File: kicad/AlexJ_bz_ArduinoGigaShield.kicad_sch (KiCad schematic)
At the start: 59 parts, among them J1 Conn_01x08, J10 JSIDE_5V, J2 Conn_01x10, J3 Conn_01x08, J4 Conn_01x08, J5 Conn_01x26, J6 Conn_01x08, J7 Conn_01x08, J8 Conn_01x26, J9 JSIDE, U1 TXB0108PW, U2 TXB0108PW, U3 TXB0108PW, U4 TXB0108PW, U5 TXB0108PW, U6 TXB0108PW, U7 TXB0108PW, U8 TXB0108PW, U9 TXB0108PW

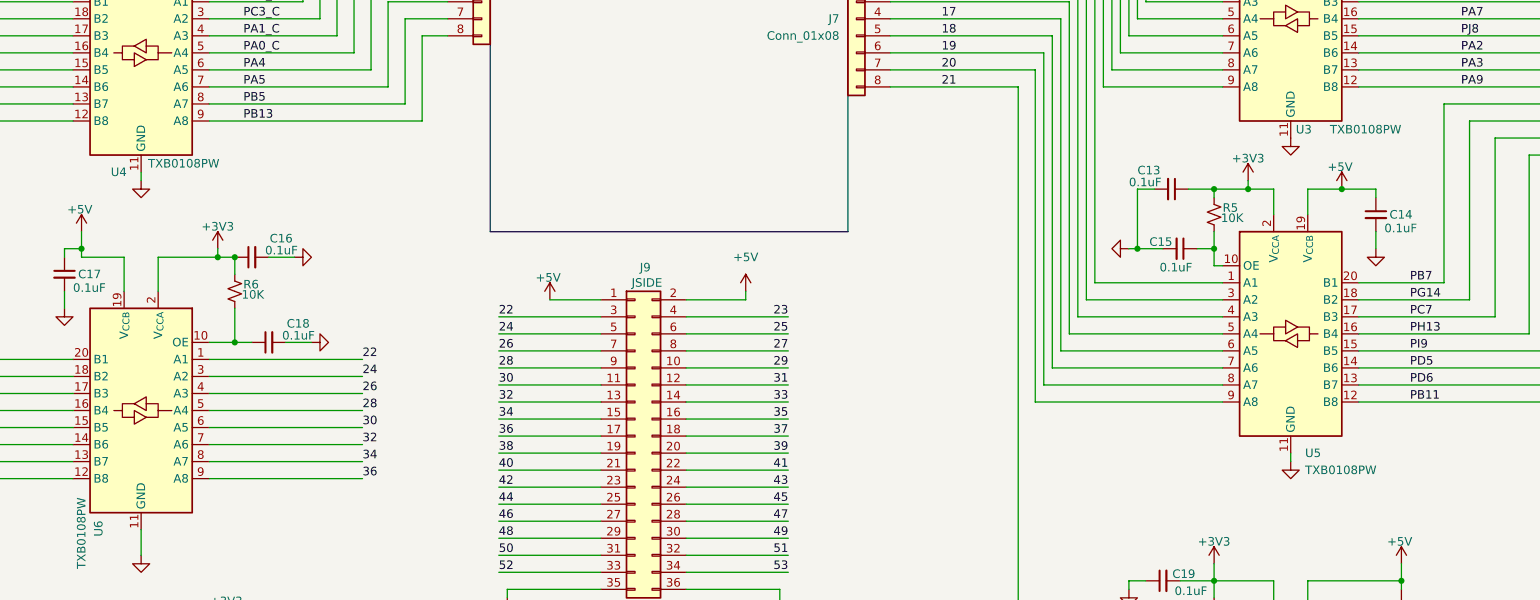
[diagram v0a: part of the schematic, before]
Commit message: Update KiCad schematic and PCB annotations for v0.2 IC replacements
Schematic: Update Value, Datasheet, and Description properties on U1-U5
to reflect new IC types (SN74LVC541, SN74AHCT541, SN74LVC4245A).
Update U5 Footprint property to TSSOP-24.

PCB: Update Value, Datasheet, and Description on U1-U5 footprints.
Update U5 footprint reference to TSSOP-24. Change silkscreen from
V0.1 to V0.2.

Note: lib_symbol definitions, pin mappings, footprint geometry, and
trace routing still reference TXB0108PW and must be updated in
KiCad GUI. See CHANGES-V0.2.md for full implementation guide.
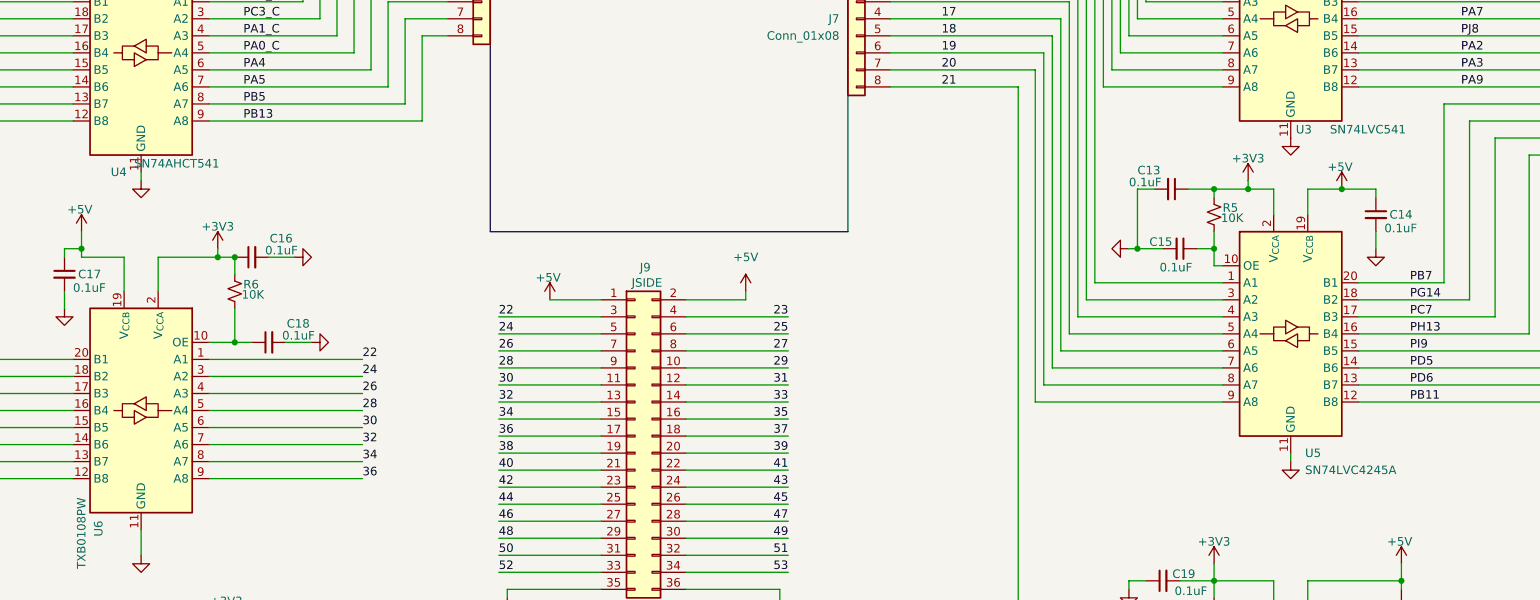
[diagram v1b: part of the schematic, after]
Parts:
- U1, U2, U3: value TXB0108PW -> SN74LVC541
- U4: value TXB0108PW -> SN74AHCT541
- U5: value TXB0108PW -> SN74LVC4245A; footprint Package_SO:TSSOP-20_4.4x6.5mm_P0.65mm -> Package_SO:TSSOP-24_4.4x7.8mm_P0.65mm
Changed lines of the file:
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@@
 			)
 		)
-		(property "Value" "TXB0108PW"
+		(property "Value" "SN74LVC541"
 			(at 100.7267 88.9 0)
 			(effects
@@
 			)
 		)
-		(property "Datasheet" "http://www.ti.com/lit/ds/symlink/txb0108.pdf"
+		(property "Datasheet" "https://www.ti.com/lit/ds/symlink/sn74lvc541a.pdf"
 			(at 102.87 71.12 0)
 			(effects
@@
 			)
 		)
-		(property "Description" "8-Bit Bidirectional Voltage-Level Translator, Auto Direction Sensing and ±15-kV ESD Protection, 1.2 - 3.6V APort, 1.65 - 5.5V BPort, TSSOP-20"
+		(property "Description" "Octal Buffer/Driver With 3-State Outputs, 5V-Tolerant Inputs, TSSOP-20 (v0.2: replaces TXB0108PW for address bus A8-A15)"
 			(at 102.87 68.58 0)
 			(effects
@@
 			)
 		)
-		(property "Value" "TXB0108PW"
+		(property "Value" "SN74LVC541"
 			(at 275.1933 86.36 0)
 			(effects
@@
 			)
 		)
-		(property "Datasheet" "http://www.ti.com/lit/ds/symlink/txb0108.pdf"
+		(property "Datasheet" "https://www.ti.com/lit/ds/symlink/sn74lvc541a.pdf"
 			(at 273.05 68.58 0)
 			(effects
@@
 			)
 		)
-		(property "Description" "8-Bit Bidirectional Voltage-Level Translator, Auto Direction Sensing and ±15-kV ESD Protection, 1.2 - 3.6V APort, 1.65 - 5.5V BPort, TSSOP-20"
+		(property "Description" "Octal Buffer/Driver With 3-State Outputs, 5V-Tolerant Inputs, TSSOP-20 (v0.2: replaces TXB0108PW for address bus A0-A7)"
 			(at 273.05 66.04 0)
 			(effects
@@
 			)
 		)
-		(property "Value" "TXB0108PW"
+		(property "Value" "SN74LVC541"
 			(at 278.892 128.27 0)
 			(effects
@@
 			)
 		)
-		(property "Datasheet" "http://www.ti.com/lit/ds/symlink/txb0108.pdf"
+		(property "Datasheet" "https://www.ti.com/lit/ds/symlink/sn74lvc541a.pdf"
 			(at 273.05 114.3 0)
 			(effects
@@
 			)
 		)
-		(property "Description" "8-Bit Bidirectional Voltage-Level Translator, Auto Direction Sensing and ±15-kV ESD Protection, 1.2 - 3.6V APort, 1.65 - 5.5V BPort, TSSOP-20"
+		(property "Description" "Octal Buffer/Driver With 3-State Outputs, 5V-Tolerant Inputs, TSSOP-20 (v0.2: replaces TXB0108PW for control inputs MREQ/IORQ/RD/WR)"
 			(at 273.05 111.76 0)
 			(effects
@@
 			)
 		)
-		(property "Value" "TXB0108PW"
+		(property "Value" "SN74LVC4245A"
 			(at 275.1933 179.07 0)
 			(effects
@@
 			)
 		)
-		(property "Footprint" "Package_SO:TSSOP-20_4.4x6.5mm_P0.65mm"
+		(property "Footprint" "Package_SO:TSSOP-24_4.4x7.8mm_P0.65mm"
 			(at 273.05 177.8 0)
 			(effects
@@
 			)
 		)
-		(property "Datasheet" "http://www.ti.com/lit/ds/symlink/txb0108.pdf"
+		(property "Datasheet" "https://www.ti.com/lit/ds/symlink/sn74lvc4245a.pdf"
 			(at 273.05 161.29 0)
 			(effects
@@
 			)
 		)
-		(property "Description" "8-Bit Bidirectional Voltage-Level Translator, Auto Direction Sensing and ±15-kV ESD Protection, 1.2 - 3.6V APort, 1.65 - 5.5V BPort, TSSOP-20"
+		(property "Description" "8-Bit Dual-Supply Bus Transceiver With Configurable Voltage Translation and 3-State Outputs, TSSOP-24 (v0.2: replaces TXB0108PW for data bus D0-D7, DIR pin on Arduino D2)"
 			(at 273.05 158.75 0)
 			(effects
@@
 			)
 		)
-		(property "Value" "TXB0108PW"
+		(property "Value" "SN74AHCT541"
 			(at 113.284 133.35 0)
 			(effects
@@
 			)
 		)
-		(property "Datasheet" "http://www.ti.com/lit/ds/symlink/txb0108.pdf"
+		(property "Datasheet" "https://www.ti.com/lit/ds/symlink/sn74ahct541.pdf"
 			(at 101.6 119.38 0)
 			(effects
@@
 			)
 		)
-		(property "Description" "8-Bit Bidirectional Voltage-Level Translator, Auto Direction Sensing and ±15-kV ESD Protection, 1.2 - 3.6V APort, 1.65 - 5.5V BPort, TSSOP-20"
+		(property "Description" "Octal Buffer/Driver With 3-State Outputs, TTL-Compatible Inputs, TSSOP-20 (v0.2: replaces TXB0108PW for control outputs CLK/RESET/INT/NMI)"
 			(at 101.6 116.84 0)
 			(effects

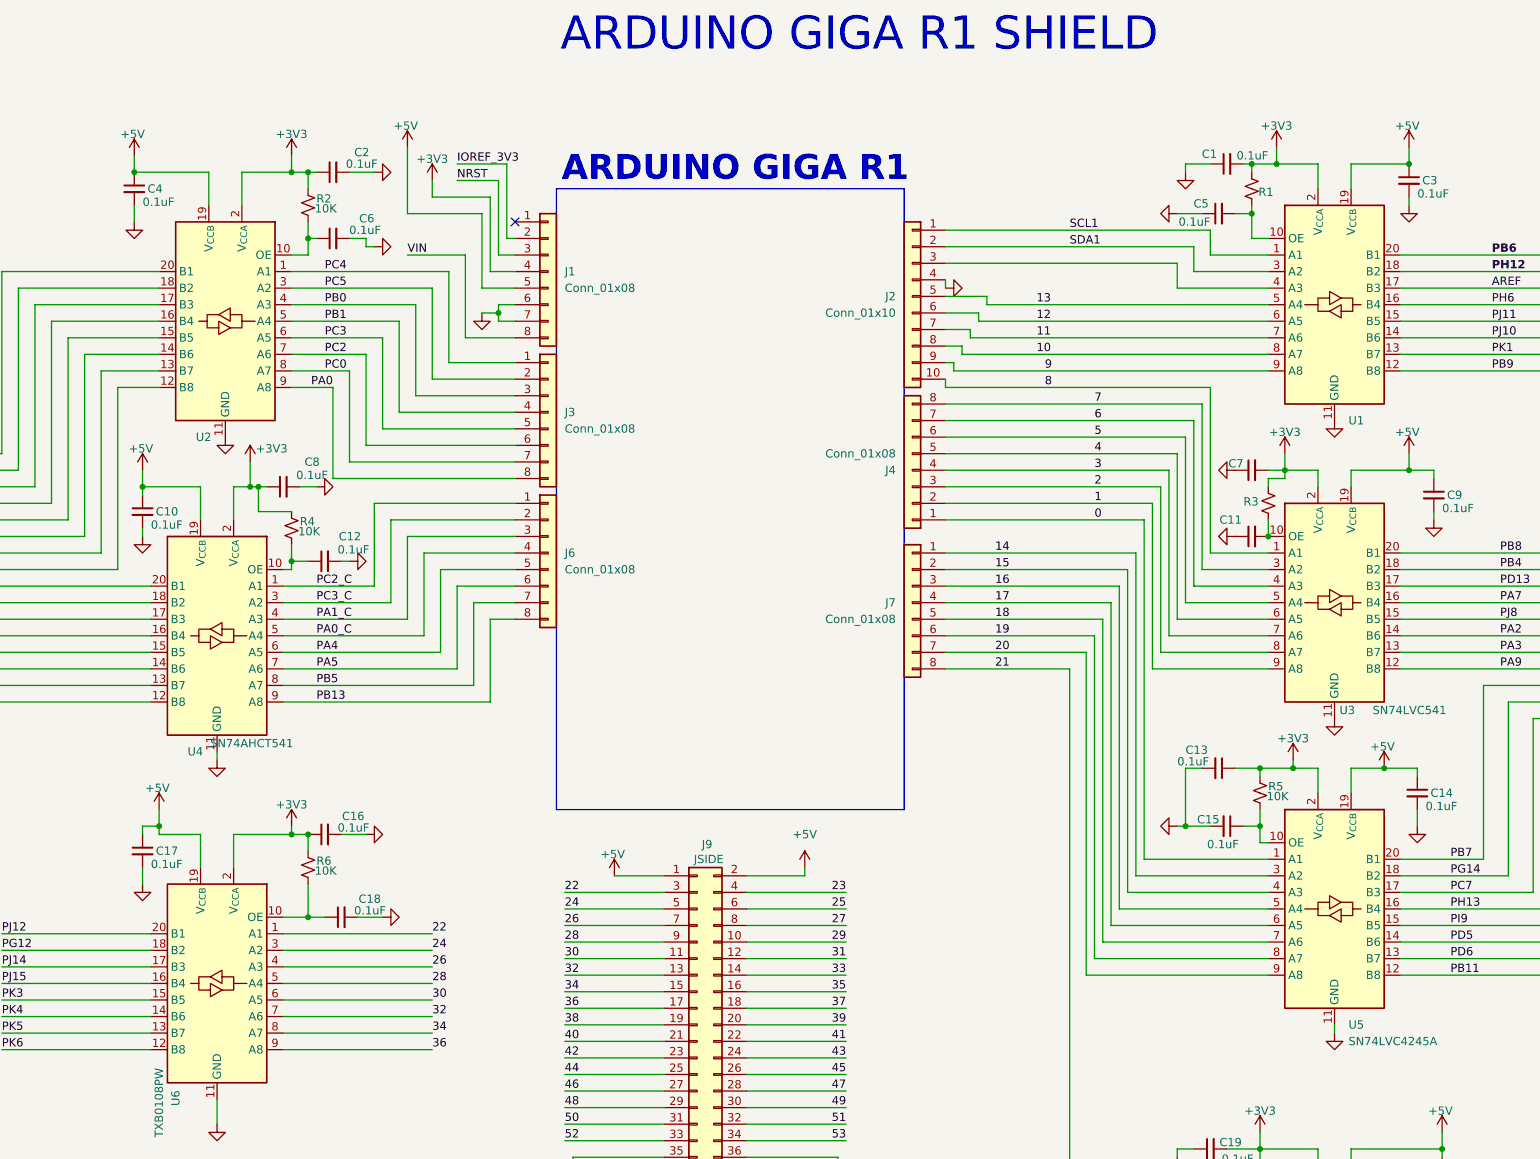
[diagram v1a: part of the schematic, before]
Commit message: v0.2 schematic: replace U1-U5 with purpose-matched level translators
- Replace U1-U3 lib_symbols from TXB0108PW to SN74LVC541 (address bus + control inputs)
- Replace U4 lib_symbol to SN74AHCT541 (control outputs)
- Replace U5 lib_symbol to SN74LVC4245A (bidirectional data bus with DIR)
- Add lib_symbol definitions for SN74LVC541, SN74AHCT541, SN74LVC4245A
- Remove R1-R5 pull-up resistors (OE pins now tied to GND)
- Add GND symbols at 1OE and 2OE pins for U1-U4
- Add GND at U5 OE_N pin (new bottom pin on TSSOP-24)
- Add DATA_DIR net label at U5 DIR pin for Arduino D2 connection
- Change U4 VCC from +3V3 to +5V (AHCT541 runs on 5V rail)
- Replace +5V with GND at VCCB/2OE positions for U1-U3
- Update silkscreen from V0.1 to V0.2
- Update Value/Description/Datasheet properties on U1-U5

Note: C19-C27 (extra decoupling caps) remain in schematic but are
excluded from BOM/CPL. Final cleanup requires KiCad GUI for trace
rerouting, footprint updates, and cap removal.
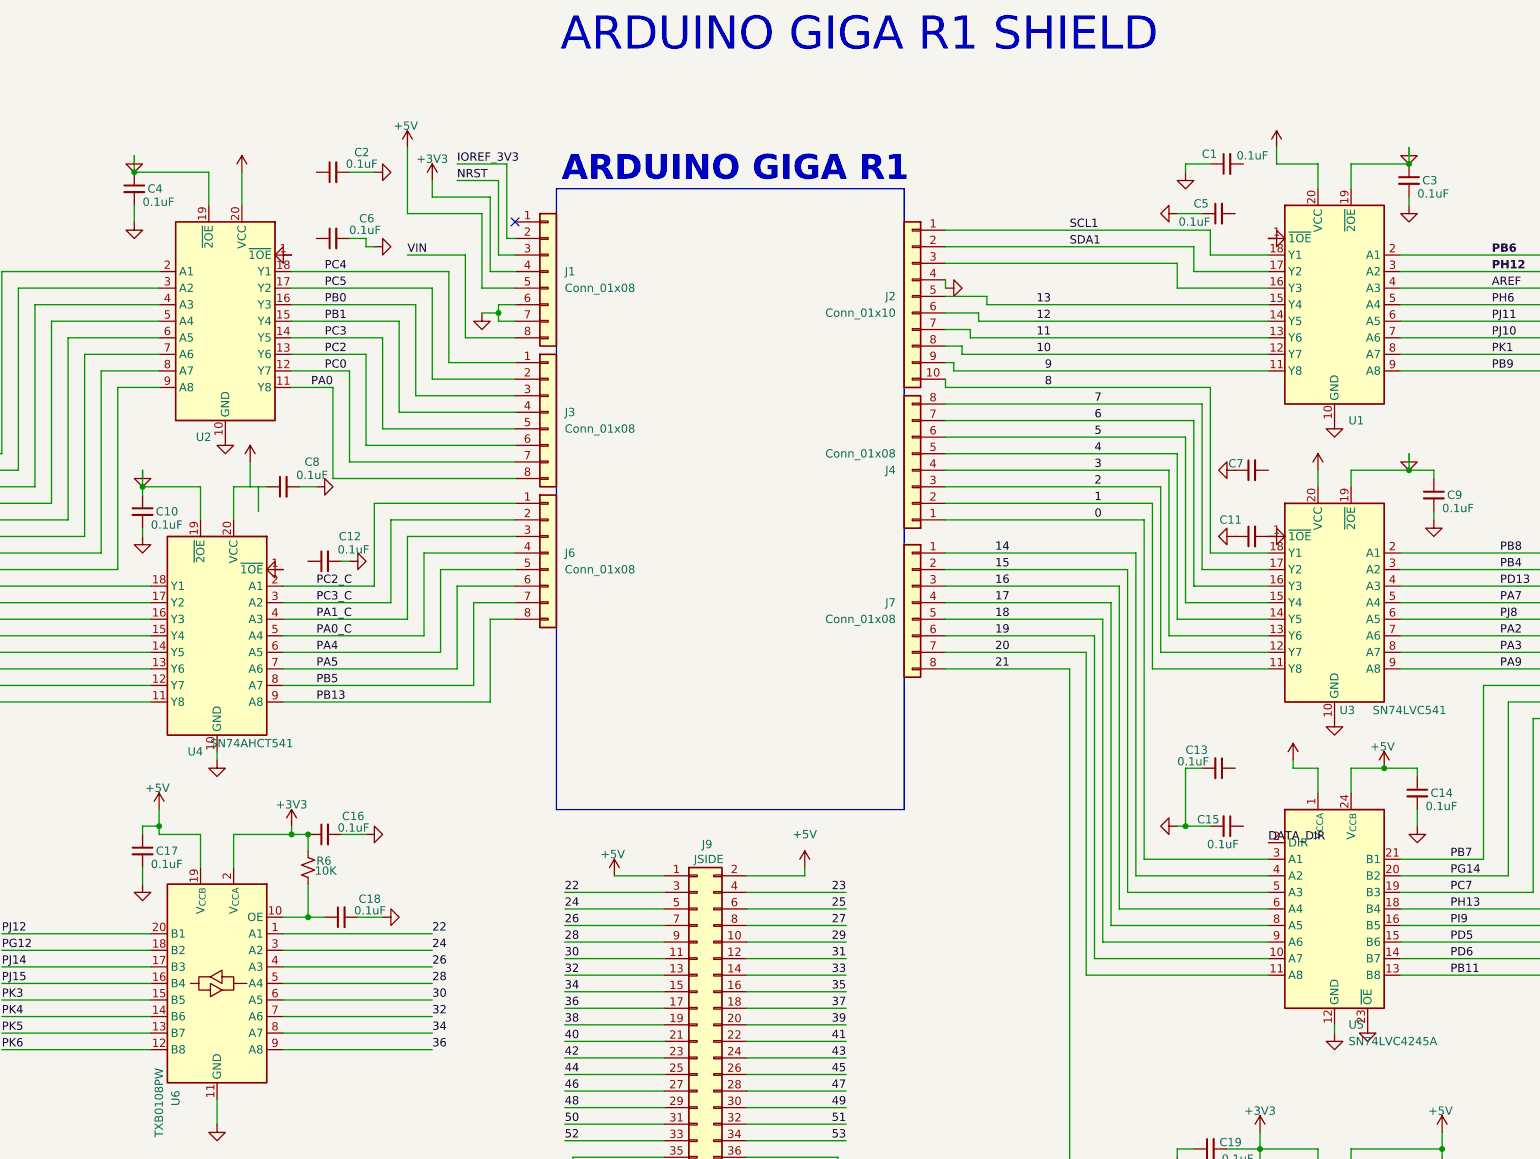
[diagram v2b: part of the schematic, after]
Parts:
- removed R1, R2, R3, R4, R5: 10K, Resistor_SMD:R_0603_1608Metric, symbol Device:R_Small_US
- U1, U2, U3: symbol Logic_LevelTranslator:TXB0108PW -> 74xx:SN74LVC541
- U4: symbol Logic_LevelTranslator:TXB0108PW -> 74xx:SN74AHCT541
- U5: symbol Logic_LevelTranslator:TXB0108PW -> 74xx:SN74LVC4245A
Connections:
- net +3V3: now also U1.20 (VCC), U2.20 (VCC), U3.20 (VCC), U5.1 (V_{CCA}); no longer C1.2, C13.1, C2.1, C7.2, C8.1, U1.2 (V_{CCA}), U2.2 (V_{CCA}), U3.2 (V_{CCA}), U4.2 (V_{CCA}), U5.2 (V_{CCA})
- net +5V: now also C8.1, U4.20 (VCC), U5.24 (V_{CCB}); no longer C10.1, C3.1, C4.1, C9.1, U1.19 (V_{CCB}), U2.19 (V_{CCB}), U3.19 (V_{CCB}), U4.19 (V_{CCB}), U5.19 (V_{CCB})
- net 0: now also U5.3 (A1); no longer U5.1 (A1)
- net 1: now also U3.11 (Y8); no longer U3.9 (A8)
- net 10: now also U1.12 (Y7); no longer U1.8 (A7)
- net 11: now also U1.13 (Y6); no longer U1.7 (A6)
- net 12: now also U1.14 (Y5); no longer U1.6 (A5)
- net 13: now also U1.15 (Y4); no longer U1.5 (A4)
- net 14: now also U5.4 (A2); no longer U5.3 (A2)
- net 15: now also U5.5 (A3); no longer U5.4 (A3)
- net 16: now also U5.6 (A4); no longer U5.5 (A4)
- net 17: now also U5.8 (A5); no longer U5.6 (A5)
- net 18: now also U5.9 (A6); no longer U5.7 (A6)
- net 19: now also U5.10 (A7); no longer U5.8 (A7)
- net 2: now also U3.12 (Y7); no longer U3.8 (A7)
- net 20: now also U5.11 (A8); no longer U5.9 (A8)
- net 3: now also U3.13 (Y6); no longer U3.7 (A6)
- net 4: now also U3.14 (Y5); no longer U3.6 (A5)
- net 5: now also U3.15 (Y4); no longer U3.5 (A4)
- net 6: now also U3.16 (Y3); no longer U3.4 (A3)
- net 7: now also U3.17 (Y2); no longer U3.3 (A2)
- net 8: now also U3.18 (Y1); no longer U3.1 (A1)
- net 9: now also U1.11 (Y8); no longer U1.9 (A8)
- net A0: now also U2.2 (A1); no longer U2.20 (B1)
- net A1: now also U2.3 (A2); no longer U2.18 (B2)
- net A10: now also U4.16 (Y3); no longer U4.17 (B3)
- net A11: now also U4.15 (Y4); no longer U4.16 (B4)
- net A2: now also U2.4 (A3); no longer U2.17 (B3)
- net A3: now also U2.5 (A4); no longer U2.16 (B4)
- net A4: now also U2.6 (A5); no longer U2.15 (B5)
- net A5: now also U2.7 (A6); no longer U2.14 (B6)
- net A6: now also U2.8 (A7); no longer U2.13 (B7)
- net A7: now also U2.9 (A8); no longer U2.12 (B8)
- net A8: now also U4.18 (Y1); no longer U4.20 (B1)
- net A9: now also U4.17 (Y2); no longer U4.18 (B2)
- net AREF: now also U1.4 (A3); no longer U1.17 (B3)
- net CAN_RX: now also U4.12 (Y7); no longer U4.13 (B7)
- net CAN_TX: now also U4.11 (Y8); no longer U4.12 (B8)
- net DAC0: now also U4.14 (Y5); no longer U4.15 (B5)
- net DAC1: now also U4.13 (Y6); no longer U4.14 (B6)
- net GND: now also C10.1, C11.2, C3.1, C4.1, C9.1, U1.1 (~{1OE}), U1.10 (GND), U1.19 (~{2OE}), U2.1 (~{1OE}), U2.10 (GND), U2.19 (~{2OE}), U3.1 (~{1OE}), U3.10 (GND), U3.19 (~{2OE}), U4.1 (~{1OE}), U4.10 (GND), U4.19 (~{2OE}), U5.12 (GND), U5.23 (~{OE}); no longer U1.11 (GND), U2.11 (GND), U3.11 (GND), U4.11 (GND), U5.11 (GND)
- net PA0: now also U2.11 (Y8); no longer U2.9 (A8)
- net PA2: now also U3.7 (A6); no longer U3.14 (B6)
- net PA3: now also U3.8 (A7); no longer U3.13 (B7)
- net PA7: now also U3.5 (A4); no longer U3.16 (B4)
- net PA9: now also U3.9 (A8); no longer U3.12 (B8)
- net PB0: now also U2.16 (Y3); no longer U2.4 (A3)
- net PB1: now also U2.15 (Y4); no longer U2.5 (A4)
- net PB11: now also U5.13 (B8); no longer U5.12 (B8)
- net PB4: now also U3.3 (A2); no longer U3.18 (B2)
- net PB6: now also U1.2 (A1); no longer U1.20 (B1)
- net PB7: now also U5.21 (B1); no longer U5.20 (B1)
- net PB8: now also U3.2 (A1); no longer U3.20 (B1)
- net PB9: now also U1.9 (A8); no longer U1.12 (B8)
- net PC0: now also U2.12 (Y7); no longer U2.8 (A7)
- net PC2: now also U2.13 (Y6); no longer U2.7 (A6)
- net PC2_C: now also U4.2 (A1); no longer U4.1 (A1)
- net PC3: now also U2.14 (Y5); no longer U2.6 (A5)
- net PC4: now also U2.18 (Y1); no longer U2.1 (A1)
- net PC5: now also U2.17 (Y2); no longer U2.3 (A2)
- net PC7: now also U5.19 (B3); no longer U5.17 (B3)
- net PD13: now also U3.4 (A3); no longer U3.17 (B3)
- net PD5: now also U5.15 (B6); no longer U5.14 (B6)
- net PD6: now also U5.14 (B7); no longer U5.13 (B7)
- net PG14: now also U5.20 (B2); no longer U5.18 (B2)
- net PH12: now also U1.3 (A2); no longer U1.18 (B2)
- net PH13: now also U5.18 (B4); no longer U5.16 (B4)
- net PH6: now also U1.5 (A4); no longer U1.16 (B4)
- net PI9: now also U5.16 (B5); no longer U5.15 (B5)
- net PJ10: now also U1.7 (A6); no longer U1.14 (B6)
- net PJ11: now also U1.6 (A5); no longer U1.15 (B5)
- net PJ8: now also U3.6 (A5); no longer U3.15 (B5)
- net PK1: now also U1.8 (A7); no longer U1.13 (B7)
- net SCL1: now also U1.18 (Y1); no longer U1.1 (A1)
- net SDA1: now also U1.17 (Y2); no longer U1.3 (A2)
- net at C6.1: no longer U2.10 (OE)
- net at C5.2: no longer U1.10 (OE)
- net at J2.3 (Pin_3): now also U1.16 (Y3); no longer U1.4 (A3)
- net at C15.1: no longer U5.10 (OE)
- net at C12.1: no longer U4.10 (OE)
- new net DATA_DIR: U5.2 (DIR)
